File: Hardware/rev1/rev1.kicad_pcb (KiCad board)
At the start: 4 copper layers, 80 x 22 mm, 43 parts, among them J1 Conn_ARM_JTAG_SWD_10, J2 USB_C_Receptacle_USB2.0_14P, J3 Screw_Terminal_01x02, J6 Conn_01x09_Socket, Q1 AO3400A, SW1 SW_Push, U1 W25Q128JVS, U2 HT75xx-1-SOT89, U3 MS5607-02BA, U4 STM32F103C8Tx, Y1 16MHz

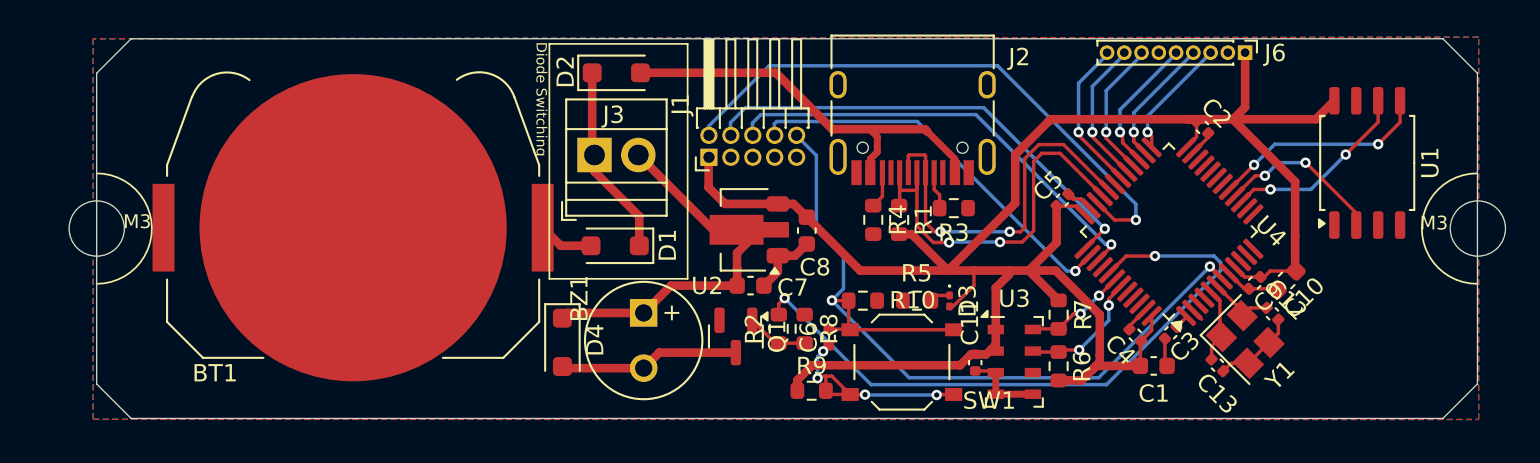
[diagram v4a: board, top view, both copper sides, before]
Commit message: Updated traces, moved mounting hole, selected switching diodes for power regulation
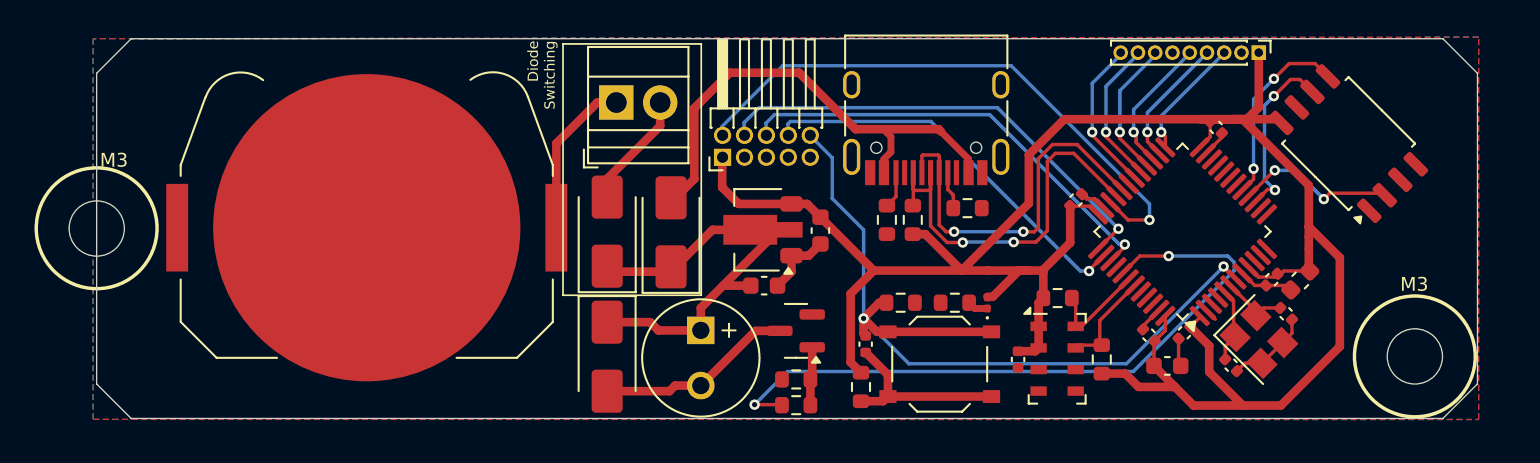
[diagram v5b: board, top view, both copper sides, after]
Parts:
- D1, D2: value D -> SS54; footprint Diode_SMD:D_SOD-123F -> Diode_SMD:D_SMA
- D4: value SM4007 -> SS54; footprint Diode_SMD:D_SOD-123F -> Diode_SMD:D_SMA
- moved D2 9.77 mm to (96.2, 66.0), turned to 90 degrees
- moved H1 8.26 mm to (139.3, 73.2)
- moved R2 4.53 mm to (103.5, 76.1), turned to 180 degrees
- moved Q1 3.50 mm to (103.5, 71.8), turned to 180 degrees
- moved BZ1 3.46 mm to (98.0, 71.7)
- moved J3 3.29 mm to (93.1, 58.5)
- moved R8 2.97 mm to (103.5, 74.6), turned to 0 degrees
- moved R9 2.87 mm to (107.2, 75.0), turned to -90 degrees
- moved D4 2.72 mm to (92.5, 73.2)
- moved R6 2.53 mm to (121.2, 73.4)
- moved C11 2.49 mm to (116.3, 73.4)
- moved U3 2.49 mm to (118.6, 73.4)
- moved SW1 2.19 mm to (111.8, 73.7)
- moved D3 2.19 mm to (114.6, 70.1), turned to 90 degrees
- moved R10 2.19 mm to (109.5, 70.1)
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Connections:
- D1 pad 1: Net-(D1-K) -> VBUS
- D1 pad 2: +BATT -> Net-(D1-A)
- D2 pad 1: Net-(D1-K) -> VBUS
- J3 pad 1: Net-(D1-K) -> +BATT
- J3 pad 2: VBUS -> Net-(D1-A)
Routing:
- net Net-(D1-K): track 11.4 -> 0.00 mm
- net +3.3V: track 118.5 -> 126.1 mm
- net Net-(D1-A): track 0.00 -> 6.87 mm
- net +BATT: track 3.23 -> 9.34 mm
- net GND: track 23.1 -> 18.5 mm
- net VUSB: track 23.9 -> 28.5 mm
- net Net-(C6-Pad1): track 12.9 -> 10.8 mm, vias 4 -> 0
- net /Microcontroller/SPI1.MOSI: track 12.8 -> 11.0 mm
- net /Microcontroller/I2C2.SDA: track 7.68 -> 5.92 mm, vias 2 -> 0
- net VBUS: track 25.4 -> 27.2 mm
- net /Microcontroller/SPI1.MISO: track 9.73 -> 11.4 mm
- net /Microcontroller/BUZZER: track 38.7 -> 40.1 mm
- net Net-(BZ1--): track 10.5 -> 11.5 mm
- net /Microcontroller/SPI1.SCLK: track 11.1 -> 10.4 mm
- net /Microcontroller/DBG.NRESET: track 48.4 -> 47.7 mm
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
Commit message: moved some hings, need to protect the oscillator n stitch and assign parts then gem
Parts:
- moved C9 0.51 mm to (131.6, 68.8)
- moved NT1 0.47 mm to (133.6, 67.6)
- moved C10 0.45 mm to (133.1, 68.9)
- moved C1 0.16 mm to (125.0, 73.9)
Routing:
- net +3.3V: track 126.1 -> 111.3 mm
- net GND: track 18.5 -> 19.3 mm
- net +3.3VA: track 3.92 -> 4.50 mm
- net /Microcontroller/I2C2.SDA: track 5.92 -> 6.10 mm, vias 0 -> 2
- net /Microcontroller/I2C2.SCK: track 5.94 -> 5.95 mm, vias 0 -> 2
- added copper zone on F.Cu, net +3.3V
